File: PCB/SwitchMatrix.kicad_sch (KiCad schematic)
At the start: 94 parts

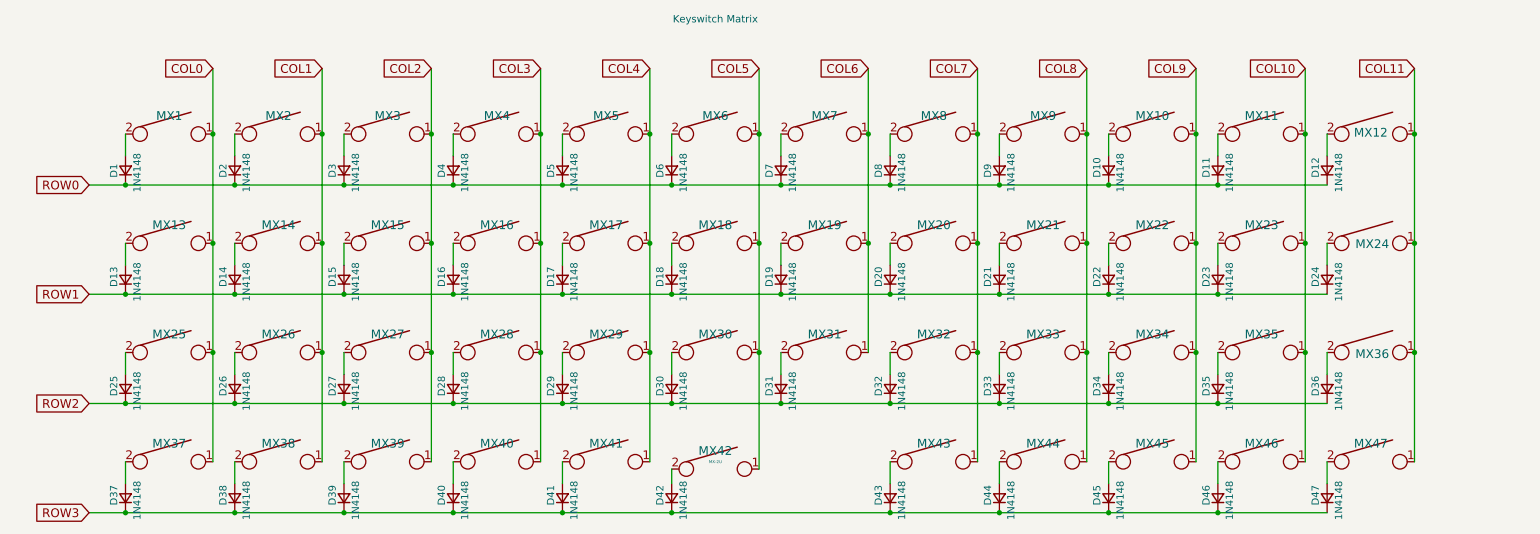
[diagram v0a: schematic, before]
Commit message: reorg symbols to be locally stored
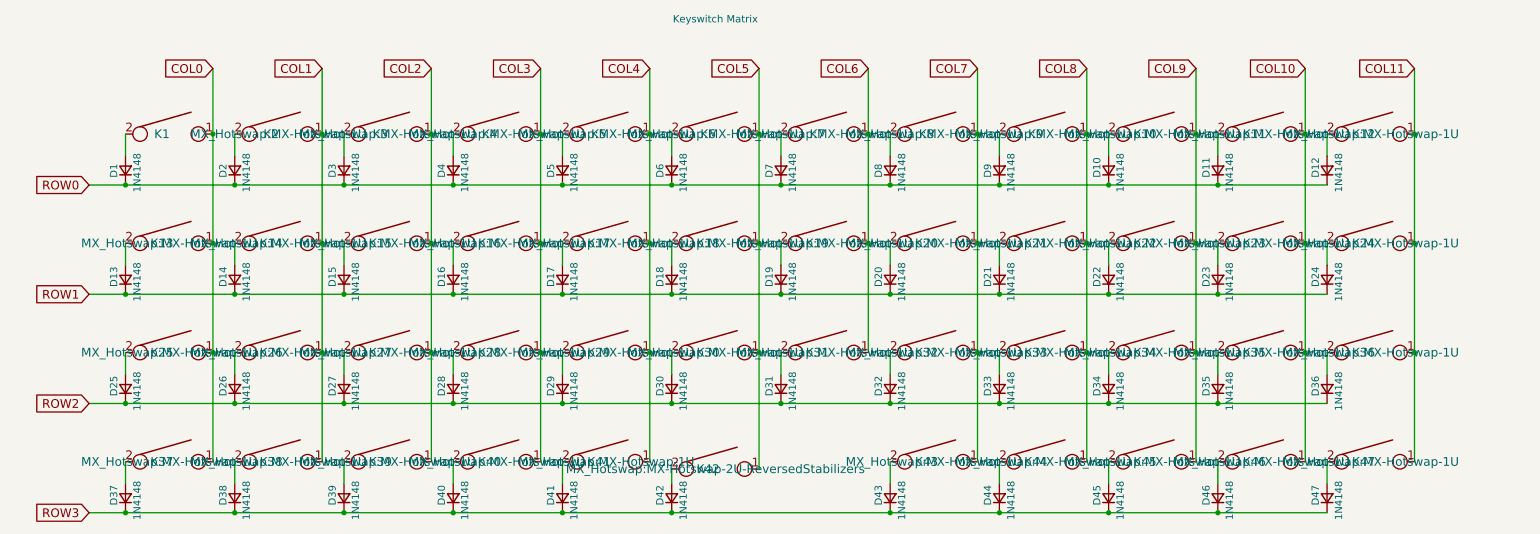
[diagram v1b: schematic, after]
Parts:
- K1: renamed from MX1; value MX-1U -> KEYSW; symbol keyboard_parts:KEYSW -> Local-lib:KEYSW
- K10: renamed from MX10; value MX-1U -> KEYSW; symbol keyboard_parts:KEYSW -> Local-lib:KEYSW
- K11: renamed from MX11; value MX-1U -> KEYSW; symbol keyboard_parts:KEYSW -> Local-lib:KEYSW
- K12: renamed from MX12; value MX-1U -> KEYSW; symbol keyboard_parts:KEYSW -> Local-lib:KEYSW
- K13: renamed from MX13; value MX-1U -> KEYSW; symbol keyboard_parts:KEYSW -> Local-lib:KEYSW
- K14: renamed from MX14; value MX-1U -> KEYSW; symbol keyboard_parts:KEYSW -> Local-lib:KEYSW
- K15: renamed from MX15; value MX-1U -> KEYSW; symbol keyboard_parts:KEYSW -> Local-lib:KEYSW
- K16: renamed from MX16; value MX-1U -> KEYSW; symbol keyboard_parts:KEYSW -> Local-lib:KEYSW
- K17: renamed from MX17; value MX-1U -> KEYSW; symbol keyboard_parts:KEYSW -> Local-lib:KEYSW
- K18: renamed from MX18; value MX-1U -> KEYSW; symbol keyboard_parts:KEYSW -> Local-lib:KEYSW
- K19: renamed from MX19; value MX-1U -> KEYSW; symbol keyboard_parts:KEYSW -> Local-lib:KEYSW
- K2: renamed from MX2; value MX-1U -> KEYSW; symbol keyboard_parts:KEYSW -> Local-lib:KEYSW
- K20: renamed from MX20; value MX-1U -> KEYSW; symbol keyboard_parts:KEYSW -> Local-lib:KEYSW
- K21: renamed from MX21; value MX-1U -> KEYSW; symbol keyboard_parts:KEYSW -> Local-lib:KEYSW
- K22: renamed from MX22; value MX-1U -> KEYSW; symbol keyboard_parts:KEYSW -> Local-lib:KEYSW
- K23: renamed from MX23; value MX-1U -> KEYSW; symbol keyboard_parts:KEYSW -> Local-lib:KEYSW
- K24: renamed from MX24; value MX-1U -> KEYSW; symbol keyboard_parts:KEYSW -> Local-lib:KEYSW
- K25: renamed from MX25; value MX-1U -> KEYSW; symbol keyboard_parts:KEYSW -> Local-lib:KEYSW
- K26: renamed from MX26; value MX-1U -> KEYSW; symbol keyboard_parts:KEYSW -> Local-lib:KEYSW
- K27: renamed from MX27; value MX-1U -> KEYSW; symbol keyboard_parts:KEYSW -> Local-lib:KEYSW
- K28: renamed from MX28; value MX-1U -> KEYSW; symbol keyboard_parts:KEYSW -> Local-lib:KEYSW
- K29: renamed from MX29; value MX-1U -> KEYSW; symbol keyboard_parts:KEYSW -> Local-lib:KEYSW
- K3: renamed from MX3; value MX-1U -> KEYSW; symbol keyboard_parts:KEYSW -> Local-lib:KEYSW
- K30: renamed from MX30; value MX-1U -> KEYSW; symbol keyboard_parts:KEYSW -> Local-lib:KEYSW
- K31: renamed from MX31; value MX-1U -> KEYSW; symbol keyboard_parts:KEYSW -> Local-lib:KEYSW
- K32: renamed from MX32; value MX-1U -> KEYSW; symbol keyboard_parts:KEYSW -> Local-lib:KEYSW
- K33: renamed from MX33; value MX-1U -> KEYSW; symbol keyboard_parts:KEYSW -> Local-lib:KEYSW
- K34: renamed from MX34; value MX-1U -> KEYSW; symbol keyboard_parts:KEYSW -> Local-lib:KEYSW
- K35: renamed from MX35; value MX-1U -> KEYSW; symbol keyboard_parts:KEYSW -> Local-lib:KEYSW
- K36: renamed from MX36; value MX-1U -> KEYSW; symbol keyboard_parts:KEYSW -> Local-lib:KEYSW
- K37: renamed from MX37; value MX-1U -> KEYSW; symbol keyboard_parts:KEYSW -> Local-lib:KEYSW
- K38: renamed from MX38; value MX-1U -> KEYSW; symbol keyboard_parts:KEYSW -> Local-lib:KEYSW
- K39: renamed from MX39; value MX-1U -> KEYSW; symbol keyboard_parts:KEYSW -> Local-lib:KEYSW
- K4: renamed from MX4; value MX-1U -> KEYSW; symbol keyboard_parts:KEYSW -> Local-lib:KEYSW
- K40: renamed from MX40; value MX-1U -> KEYSW; symbol keyboard_parts:KEYSW -> Local-lib:KEYSW
- K41: renamed from MX41; value MX-1U -> KEYSW; symbol keyboard_parts:KEYSW -> Local-lib:KEYSW
- K42: renamed from MX42; value MX-2U -> KEYSW; symbol keyboard_parts:KEYSW -> Local-lib:KEYSW
- K43: renamed from MX43; value MX-1U -> KEYSW; symbol keyboard_parts:KEYSW -> Local-lib:KEYSW
- K44: renamed from MX44; value MX-1U -> KEYSW; symbol keyboard_parts:KEYSW -> Local-lib:KEYSW
- K45: renamed from MX45; value MX-1U -> KEYSW; symbol keyboard_parts:KEYSW -> Local-lib:KEYSW
- K46: renamed from MX46; value MX-1U -> KEYSW; symbol keyboard_parts:KEYSW -> Local-lib:KEYSW
- K47: renamed from MX47; value MX-1U -> KEYSW; symbol keyboard_parts:KEYSW -> Local-lib:KEYSW
- K5: renamed from MX5; value MX-1U -> KEYSW; symbol keyboard_parts:KEYSW -> Local-lib:KEYSW
- K6: renamed from MX6; value MX-1U -> KEYSW; symbol keyboard_parts:KEYSW -> Local-lib:KEYSW
- K7: renamed from MX7; value MX-1U -> KEYSW; symbol keyboard_parts:KEYSW -> Local-lib:KEYSW
- K8: renamed from MX8; value MX-1U -> KEYSW; symbol keyboard_parts:KEYSW -> Local-lib:KEYSW
- K9: renamed from MX9; value MX-1U -> KEYSW; symbol keyboard_parts:KEYSW -> Local-lib:KEYSW

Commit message: update to use local footprints
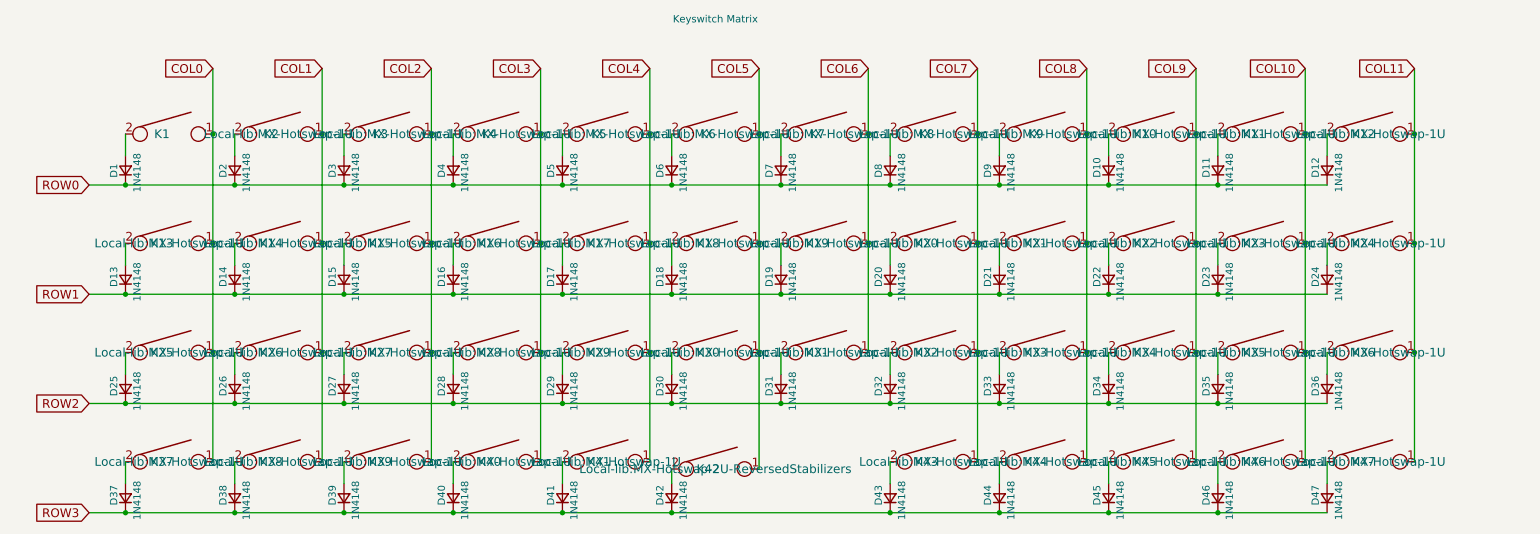
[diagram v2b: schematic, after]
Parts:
- K1, K10, K11, K12, K13, K14, K15, K16, K17, K18, K19, K2, K20, K21, K22, K23, K24, K25, K26, K27, K28, K29, K3, K30, K31, K32, K33, K34, K35, K36, K37, K38, K39, K4, K40, K41, K43, K44, K45, K46, K47, K5, K6, K7, K8, K9: footprint MX_Hotswap:MX-Hotswap-1U -> Local-lib:MX-Hotswap-1U
- K42: footprint MX_Hotswap:MX-Hotswap-2U-ReversedStabilizers -> Local-lib:MX-Hotswap-2U-ReversedStabilizers
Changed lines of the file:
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@@
 			)
 		)
-		(property "Footprint" "MX_Hotswap:MX-Hotswap-1U"
+		(property "Footprint" "Local-lib:MX-Hotswap-1U"
 			(at 204.47 124.46 0)
 			(show_name no)
@@
 			)
 		)
-		(property "Footprint" "MX_Hotswap:MX-Hotswap-1U"
+		(property "Footprint" "Local-lib:MX-Hotswap-1U"
 			(at 90.17 105.41 0)
 			(show_name no)
@@
 			)
 		)
-		(property "Footprint" "MX_Hotswap:MX-Hotswap-1U"
+		(property "Footprint" "Local-lib:MX-Hotswap-1U"
 			(at 166.37 105.41 0)
 			(show_name no)
@@
 			)
 		)
-		(property "Footprint" "MX_Hotswap:MX-Hotswap-1U"
+		(property "Footprint" "Local-lib:MX-Hotswap-1U"
 			(at 90.17 86.36 0)
 			(show_name no)
@@
 			)
 		)
-		(property "Footprint" "MX_Hotswap:MX-Hotswap-1U"
+		(property "Footprint" "Local-lib:MX-Hotswap-1U"
 			(at 52.07 86.36 0)
 			(show_name no)
@@
 			)
 		)
-		(property "Footprint" "MX_Hotswap:MX-Hotswap-1U"
+		(property "Footprint" "Local-lib:MX-Hotswap-1U"
 			(at 261.62 105.41 0)
 			(show_name no)
@@
 			)
 		)
-		(property "Footprint" "MX_Hotswap:MX-Hotswap-1U"
+		(property "Footprint" "Local-lib:MX-Hotswap-1U"
 			(at 71.12 67.31 0)
 			(show_name no)
@@
 			)
 		)
-		(property "Footprint" "MX_Hotswap:MX-Hotswap-1U"
+		(property "Footprint" "Local-lib:MX-Hotswap-1U"
 			(at 147.32 86.36 0)
 			(show_name no)
@@
 			)
 		)
-		(property "Footprint" "MX_Hotswap:MX-Hotswap-1U"
+		(property "Footprint" "Local-lib:MX-Hotswap-1U"
 			(at 71.12 124.46 0)
 			(show_name no)
@@
 			)
 		)
-		(property "Footprint" "MX_Hotswap:MX-Hotswap-1U"
+		(property "Footprint" "Local-lib:MX-Hotswap-1U"
 			(at 52.07 105.41 0)
 			(show_name no)
@@
 			)
 		)
-		(property "Footprint" "MX_Hotswap:MX-Hotswap-1U"
+		(property "Footprint" "Local-lib:MX-Hotswap-1U"
 			(at 128.27 124.46 0)
 			(show_name no)
@@
 			)
 		)
-		(property "Footprint" "MX_Hotswap:MX-Hotswap-1U"
+		(property "Footprint" "Local-lib:MX-Hotswap-1U"
 			(at 90.17 67.31 0)
 			(show_name no)
@@
 			)
 		)
-		(property "Footprint" "MX_Hotswap:MX-Hotswap-1U"
+		(property "Footprint" "Local-lib:MX-Hotswap-1U"
 			(at 147.32 105.41 0)
 			(show_name no)
@@
 			)
 		)
-		(property "Footprint" "MX_Hotswap:MX-Hotswap-1U"
+		(property "Footprint" "Local-lib:MX-Hotswap-1U"
 			(at 109.22 86.36 0)
 			(show_name no)
@@
 			)
 		)
-		(property "Footprint" "MX_Hotswap:MX-Hotswap-1U"
+		(property "Footprint" "Local-lib:MX-Hotswap-1U"
 			(at 185.42 124.46 0)
 			(show_name no)
@@
 			)
 		)
-		(property "Footprint" "MX_Hotswap:MX-Hotswap-1U"
+		(property "Footprint" "Local-lib:MX-Hotswap-1U"
 			(at 185.42 86.36 0)
 			(show_name no)
@@
 			)
 		)
-		(property "Footprint" "MX_Hotswap:MX-Hotswap-1U"
+		(property "Footprint" "Local-lib:MX-Hotswap-1U"
 			(at 223.52 105.41 0)
 			(show_name no)
@@
 			)
 		)
-		(property "Footprint" "MX_Hotswap:MX-Hotswap-1U"
+		(property "Footprint" "Local-lib:MX-Hotswap-1U"
 			(at 242.57 86.36 0)
 			(show_name no)
@@
 			)
 		)
-		(property "Footprint" "MX_Hotswap:MX-Hotswap-1U"
+		(property "Footprint" "Local-lib:MX-Hotswap-1U"
 			(at 147.32 67.31 0)
 			(show_name no)
@@
 			)
 		)
-		(property "Footprint" "MX_Hotswap:MX-Hotswap-1U"
+		(property "Footprint" "Local-lib:MX-Hotswap-1U"
 			(at 71.12 105.41 0)
 			(show_name no)
@@
 			)
 		)
-		(property "Footprint" "MX_Hotswap:MX-Hotswap-1U"
+		(property "Footprint" "Local-lib:MX-Hotswap-1U"
 			(at 109.22 124.46 0)
 			(show_name no)
@@
 			)
 		)
-		(property "Footprint" "MX_Hotswap:MX-Hotswap-1U"
+		(property "Footprint" "Local-lib:MX-Hotswap-1U"
 			(at 128.27 67.31 0)
 			(show_name no)
@@
 			)
 		)
-		(property "Footprint" "MX_Hotswap:MX-Hotswap-1U"
+		(property "Footprint" "Local-lib:MX-Hotswap-1U"
 			(at 261.62 124.46 0)
 			(show_name no)
@@
 			)
 		)
-		(property "Footprint" "MX_Hotswap:MX-Hotswap-1U"
+		(property "Footprint" "Local-lib:MX-Hotswap-1U"
 			(at 242.57 67.31 0)
 			(show_name no)
@@
 			)
 		)
-		(property "Footprint" "MX_Hotswap:MX-Hotswap-1U"
+		(property "Footprint" "Local-lib:MX-Hotswap-1U"
 			(at 185.42 67.31 0)
 			(show_name no)
@@
 			)
 		)
-		(property "Footprint" "MX_Hotswap:MX-Hotswap-1U"
+		(property "Footprint" "Local-lib:MX-Hotswap-1U"
 			(at 109.22 67.31 0)
 			(show_name no)
@@
 			)
 		)
-		(property "Footprint" "MX_Hotswap:MX-Hotswap-1U"
+		(property "Footprint" "Local-lib:MX-Hotswap-1U"
 			(at 128.27 105.41 0)
 			(show_name no)
@@
 			)
 		)
-		(property "Footprint" "MX_Hotswap:MX-Hotswap-1U"
+		(property "Footprint" "Local-lib:MX-Hotswap-1U"
 			(at 204.47 86.36 0)
 			(show_name no)
@@
 			)
 		)
-		(property "Footprint" "MX_Hotswap:MX-Hotswap-1U"
+		(property "Footprint" "Local-lib:MX-Hotswap-1U"
 			(at 109.22 105.41 0)
 			(show_name no)
@@
 			)
 		)
-		(property "Footprint" "MX_Hotswap:MX-Hotswap-1U"
+		(property "Footprint" "Local-lib:MX-Hotswap-1U"
 			(at 261.62 86.36 0)
 			(show_name no)
@@
 			)
 		)
-		(property "Footprint" "MX_Hotswap:MX-Hotswap-1U"
+		(property "Footprint" "Local-lib:MX-Hotswap-1U"
 			(at 52.07 67.31 0)
 			(hide yes)
@@
 			)
 		)
-		(property "Footprint" "MX_Hotswap:MX-Hotswap-1U"
+		(property "Footprint" "Local-lib:MX-Hotswap-1U"
 			(at 242.57 105.41 0)
 			(show_name no)
@@
 			)
 		)
-		(property "Footprint" "MX_Hotswap:MX-Hotswap-1U"
+		(property "Footprint" "Local-lib:MX-Hotswap-1U"
 			(at 166.37 67.31 0)
 			(show_name no)
@@
 			)
 		)
-		(property "Footprint" "MX_Hotswap:MX-Hotswap-1U"
+		(property "Footprint" "Local-lib:MX-Hotswap-1U"
 			(at 242.57 124.46 0)
 			(show_name no)
@@
 			)
 		)
-		(property "Footprint" "MX_Hotswap:MX-Hotswap-1U"
+		(property "Footprint" "Local-lib:MX-Hotswap-1U"
 			(at 128.27 86.36 0)
 			(show_name no)
@@
 			)
 		)
-		(property "Footprint" "MX_Hotswap:MX-Hotswap-1U"
+		(property "Footprint" "Local-lib:MX-Hotswap-1U"
 			(at 223.52 124.46 0)
 			(show_name no)
@@
 			)
 		)
-		(property "Footprint" "MX_Hotswap:MX-Hotswap-1U"
+		(property "Footprint" "Local-lib:MX-Hotswap-1U"
 			(at 223.52 86.36 0)
 			(show_name no)
@@
 			)
 		)
-		(property "Footprint" "MX_Hotswap:MX-Hotswap-1U"
+		(property "Footprint" "Local-lib:MX-Hotswap-1U"
 			(at 204.47 105.41 0)
 			(show_name no)
@@
 			)
 		)
-		(property "Footprint" "MX_Hotswap:MX-Hotswap-2U-ReversedStabilizers"
+		(property "Footprint" "Local-lib:MX-Hotswap-2U-ReversedStabilizers"
 			(at 147.32 125.73 0)
 			(show_name no)
@@
 			)
 		)
-		(property "Footprint" "MX_Hotswap:MX-Hotswap-1U"
+		(property "Footprint" "Local-lib:MX-Hotswap-1U"
 			(at 166.37 86.36 0)
 			(show_name no)
@@
 			)
 		)
-		(property "Footprint" "MX_Hotswap:MX-Hotswap-1U"
+		(property "Footprint" "Local-lib:MX-Hotswap-1U"
 			(at 52.07 124.46 0)
 			(show_name no)
@@
 			)
 		)
-		(property "Footprint" "MX_Hotswap:MX-Hotswap-1U"
+		(property "Footprint" "Local-lib:MX-Hotswap-1U"
 			(at 185.42 105.41 0)
 			(show_name no)
@@
 			)
 		)
-		(property "Footprint" "MX_Hotswap:MX-Hotswap-1U"
+		(property "Footprint" "Local-lib:MX-Hotswap-1U"
 			(at 223.52 67.31 0)
 			(show_name no)
@@
 			)
 		)
-		(property "Footprint" "MX_Hotswap:MX-Hotswap-1U"
+		(property "Footprint" "Local-lib:MX-Hotswap-1U"
 			(at 71.12 86.36 0)
 			(show_name no)
@@
 			)
 		)
-		(property "Footprint" "MX_Hotswap:MX-Hotswap-1U"
+		(property "Footprint" "Local-lib:MX-Hotswap-1U"
 			(at 90.17 124.46 0)
 			(show_name no)
@@
 			)
 		)
-		(property "Footprint" "MX_Hotswap:MX-Hotswap-1U"
+		(property "Footprint" "Local-lib:MX-Hotswap-1U"
 			(at 204.47 67.31 0)
 			(show_name no)
@@
 			)
 		)
-		(property "Footprint" "MX_Hotswap:MX-Hotswap-1U"
+		(property "Footprint" "Local-lib:MX-Hotswap-1U"
 			(at 261.62 67.31 0)
 			(show_name no)
